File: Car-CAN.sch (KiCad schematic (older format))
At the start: 18 parts, among them J19 CAN_IN, J20 CAN_OUT, J26 CAN_TP, U15 ADM3055E, U16 CDSOT23-T24CAN

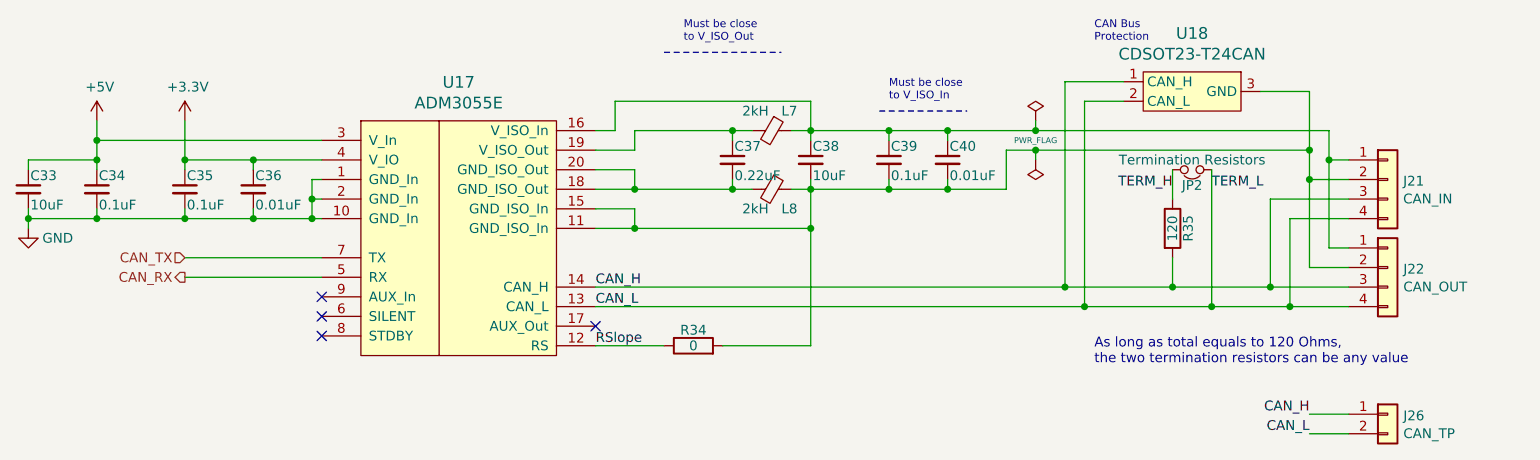
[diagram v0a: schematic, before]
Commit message: Edits schematic to make turn lights software controlled
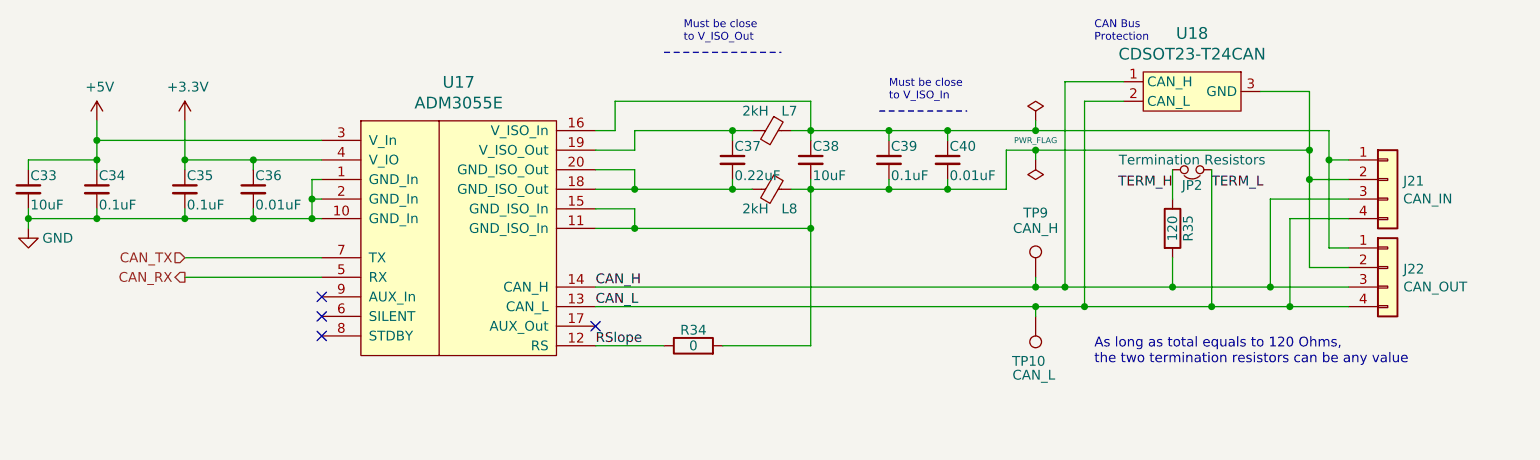
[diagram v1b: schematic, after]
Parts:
- removed J26: CAN_TP, Connector_PinHeader_2.54mm:PinHeader_1x02_P2.54mm_Vertical, symbol Connector_Generic:Conn_01x02
- added TP7: CAN_H, TestPoint:TestPoint_Keystone_5005-5009_Compact, symbol Connector:TestPoint
- added TP8: CAN_L, TestPoint:TestPoint_Keystone_5005-5009_Compact, symbol Connector:TestPoint
- J19, J20: footprint UTSVT_Connectors:Molex_MicroFit3.0_1x4xP3.00mm_PolarizingPeg_Vertical -> utsvt_conn:Molex_MicroFit3.0_1x4xP3.00mm_PolarizingPeg_Vertical
- U15: footprint UTSVT_ICs:SOIC-20W_7.5x15.4mm_Pitch1.27mm -> utsvt_ics:SOIC-20W_7.5x15.4mm_Pitch1.27mm
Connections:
- net CAN_H: now also TP7.1
- net CAN_L: now also TP8.1
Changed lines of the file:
@@
 CAN Bus\nProtection
+$Comp
+L Connector:TestPoint TP?
+U 1 1 5C2B43B6
+P 7300 3800
+AR Path="/5E5E1F90/5C2B43B6" Ref="TP?"  Part="1"
+AR Path="/5E80FF20/5C2B43B6" Ref="TP?"  Part="1"
+AR Path="/5EA71171/5C2B43B6" Ref="TP?"  Part="1"
+AR Path="/5F479052/5C2B43B6" Ref="TP7"  Part="1"
+AR Path="/5F547B94/5C2B43B6" Ref="TP9"  Part="1"
+F 0 "TP9" H 7300 4100 50  0000 C BNN
+F 1 "CAN_H" H 7300 4050 50  0000 C CNN
+F 2 "TestPoint:TestPoint_Keystone_5005-5009_Compact" H 7300 3800 50  0001 C CNN
+F 3 "" H 7300 3800 50  0001 C CNN
+	1    7300 3800
+	1    0    0    -1
+$EndComp
+$Comp
+L Connector:TestPoint TP?
+U 1 1 5C2B43BD
+P 7300 4000
+AR Path="/5E5E1F90/5C2B43BD" Ref="TP?"  Part="1"
+AR Path="/5E80FF20/5C2B43BD" Ref="TP?"  Part="1"
+AR Path="/5EA71171/5C2B43BD" Ref="TP?"  Part="1"
+AR Path="/5F479052/5C2B43BD" Ref="TP8"  Part="1"
+AR Path="/5F547B94/5C2B43BD" Ref="TP10"  Part="1"
+F 0 "TP10" H 7250 4200 50  0000 L BNN
+F 1 "CAN_L" H 7200 4300 50  0000 L CNN
+F 2 "TestPoint:TestPoint_Keystone_5005-5009_Compact" H 7300 4000 50  0001 C CNN
+F 3 "" H 7300 4000 50  0001 C CNN
+	1    7300 4000
+	-1   0    0    1
+$EndComp
 $Comp
 L Device:R R?
@@
 	6050 3050 6150 3050
 Wire Wire Line
+	7300 3800 7300 3850
+Wire Wire Line
 	5700 4150 6150 4150
 Wire Wire Line
@@
 Wire Wire Line
 	6150 3350 6550 3350
+Connection ~ 7300 3850
+Wire Wire Line
+	7300 3850 7450 3850
+Wire Wire Line
+	5050 3850 7300 3850
+Wire Wire Line
+	5050 3950 7300 3950
+Wire Wire Line
+	7300 4000 7300 3950
+Connection ~ 7300 3950
+Wire Wire Line
+	7300 3950 7550 3950
 Connection ~ 5750 3350
 Text Label 5050 3850 0    50   ~ 0
@@
 F 0 "J22" H 9180 3742 50  0000 L CNN
 F 1 "CAN_OUT" H 9180 3651 50  0000 L CNN
-F 2 "UTSVT_Connectors:Molex_MicroFit3.0_1x4xP3.00mm_PolarizingPeg_Vertical" H 9100 3750 50  0001 C CNN
+F 2 "utsvt_conn:Molex_MicroFit3.0_1x4xP3.00mm_PolarizingPeg_Vertical" H 9100 3750 50  0001 C CNN
 F 3 "~" H 9100 3750 50  0001 C CNN
 	1    9100 3750
@@
 F 0 "U17" H 4350 4397 60  0000 C CNN
 F 1 "ADM3055E" H 4350 4291 60  0000 C CNN
-F 2 "UTSVT_ICs:SOIC-20W_7.5x15.4mm_Pitch1.27mm" H 4350 3700 60  0001 C CNN
+F 2 "utsvt_ics:SOIC-20W_7.5x15.4mm_Pitch1.27mm" H 4350 3700 60  0001 C CNN
 F 3 "" H 4350 3700 60  0001 C CNN
 	1    4350 3600
@@
 F 0 "J21" H 9179 3292 50  0000 L CNN
 F 1 "CAN_IN" H 9179 3201 50  0000 L CNN
-F 2 "UTSVT_Connectors:Molex_MicroFit3.0_1x4xP3.00mm_PolarizingPeg_Vertical" H 9100 3300 50  0001 C CNN
+F 2 "utsvt_conn:Molex_MicroFit3.0_1x4xP3.00mm_PolarizingPeg_Vertical" H 9100 3300 50  0001 C CNN
 F 3 "~" H 9100 3300 50  0001 C CNN
 	1    9100 3300
@@
 Wire Wire Line
 	8200 3250 8200 3950
-$Comp
-L Connector_Generic:Conn_01x02 J?
-U 1 1 5FBD46EC
-P 9100 4500
-AR Path="/5F6018FB/5FBD46EC" Ref="J?"  Part="1"
-AR Path="/5F547B94/5FBD46EC" Ref="J26"  Part="1"
-F 0 "J26" H 9180 4492 50  0000 L CNN
-F 1 "CAN_TP" H 9180 4401 50  0000 L CNN
-F 2 "Connector_PinHeader_2.54mm:PinHeader_1x02_P2.54mm_Vertical" H 9100 4500 50  0001 C CNN
-F 3 "~" H 9100 4500 50  0001 C CNN
-	1    9100 4500
-	1    0    0    -1
-$EndComp
-Text Label 8700 4500 2    50   ~ 0
-CAN_H
-Text Label 8700 4600 2    50   ~ 0
-CAN_L
-Wire Wire Line
-	8900 4500 8700 4500
-Wire Wire Line
-	8900 4600 8700 4600
-Wire Wire Line
-	5050 3850 7450 3850
-Wire Wire Line
-	5050 3950 7550 3950
 $EndSCHEMATC
